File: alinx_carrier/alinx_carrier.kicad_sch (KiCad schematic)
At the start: 4 parts, among them J1 AXK6A2337YG, J2 AXK6A2337YG, J3 AXK6A2337YG, J4 AXK6A2337YG

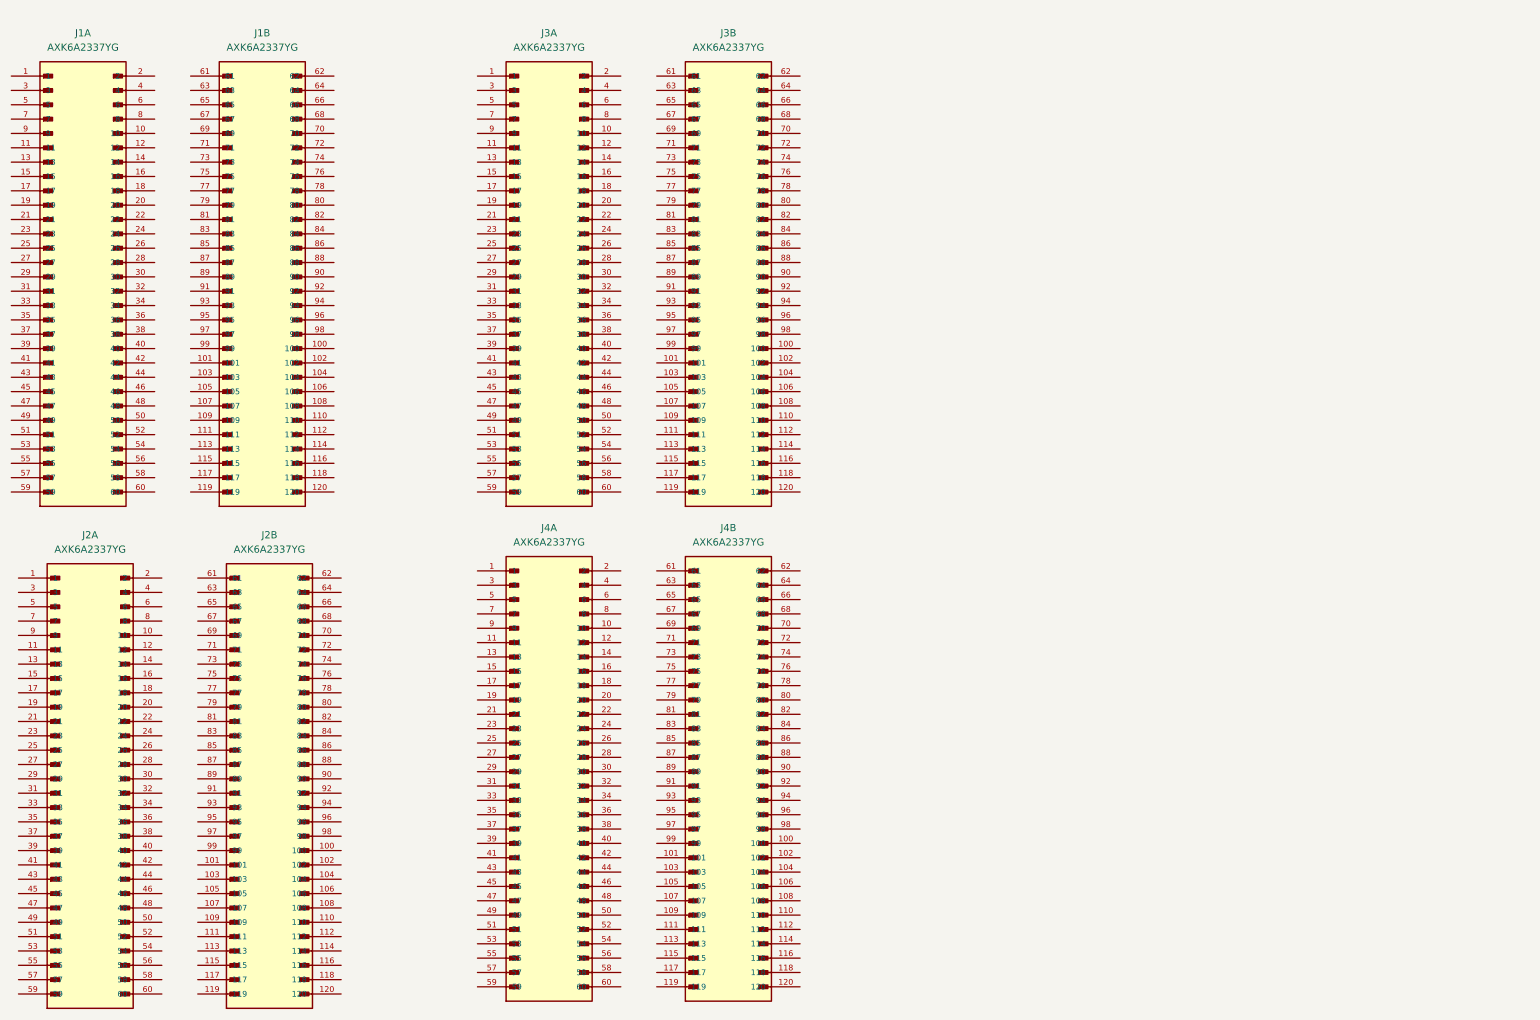
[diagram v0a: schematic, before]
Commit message: pulled in latest files froms snapeda for AXK6A2337YG
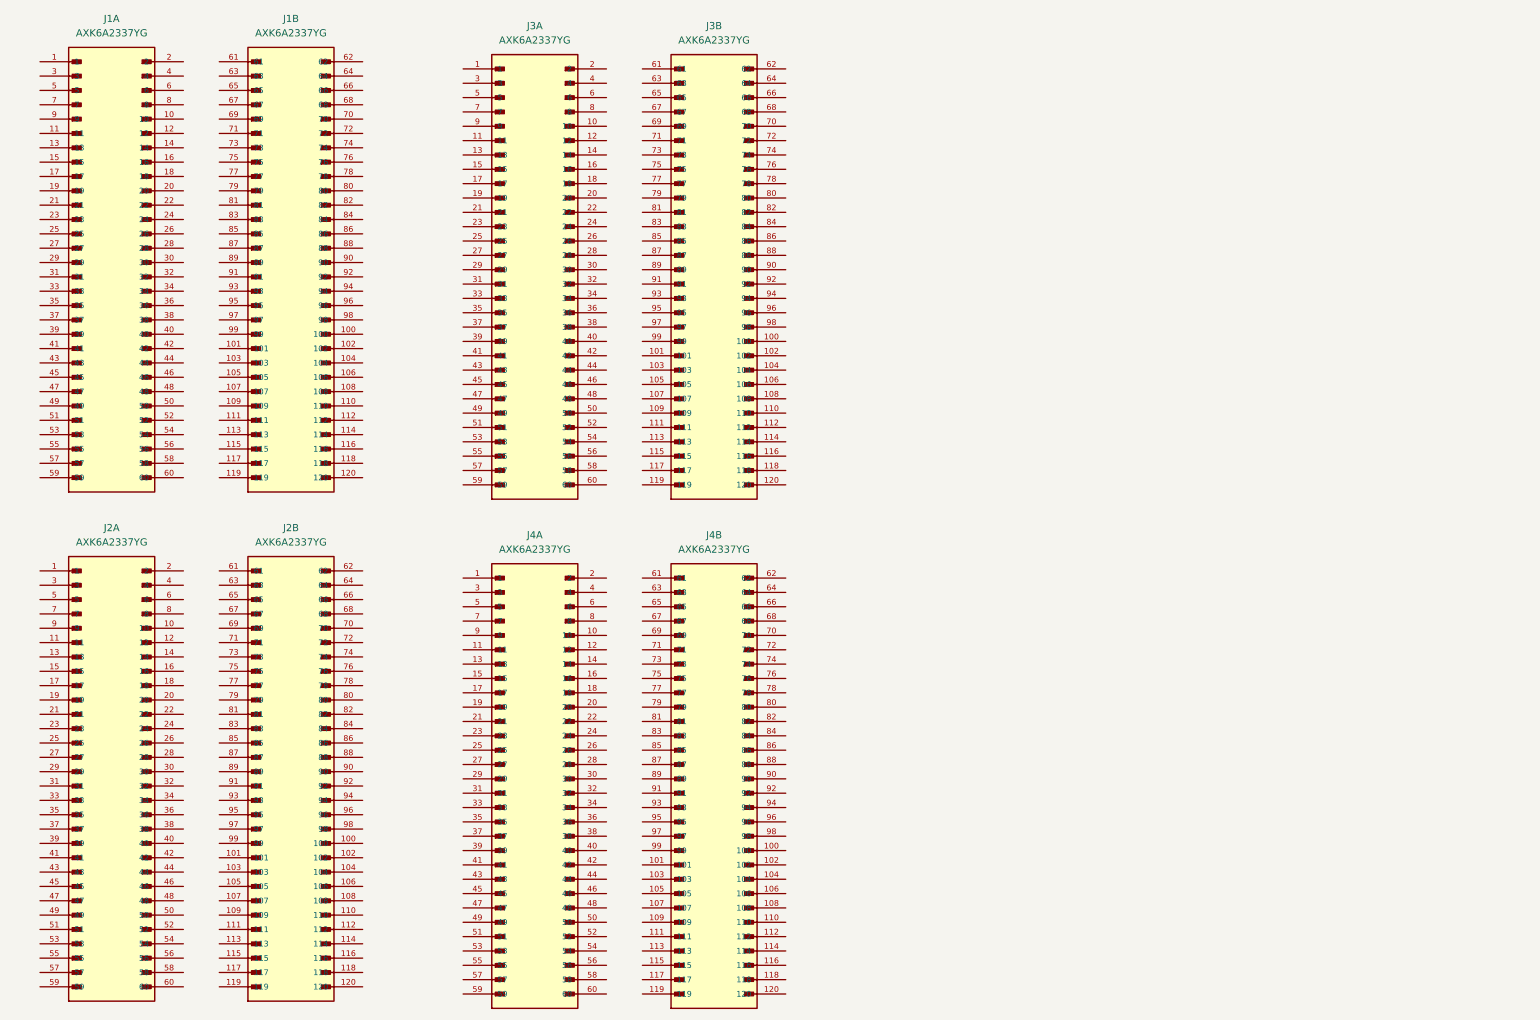
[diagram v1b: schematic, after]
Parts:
- J1, J2, J3, J4: footprint pedrolib:PANASONIC_AXK6A2337YG -> PANASONIC_AXK6A2337YG; AVAILABILITY (none) -> In Stock; DESCRIPTION (none) -> 120 Position Connector Header, Outer Shroud Contacts Surfac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; MANUFACTURER Panasonic -> (none); MAXIMUM_PACKAGE_HEIGHT 2.6mm -> (none); MF (none) -> Panasonic; MP (none) -> AXK6A2337YG; PACKAGE (none) -> None; PARTREV 2022.4 -> (none); PRICE (none) -> None; PURCHASE-URL (none) -> https://pricing.snapeda.com/search/part/AXK6A2337YG/?ref=eda; SNAPEDA_PN AXK6A2337YG -> (none); STANDARD Manufacturer Recommendations -> (none)

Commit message: added mounting holes to alinx carrier
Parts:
- added H1, H2, H3, H4: MountingHole_Pad, MountingHole:MountingHole_3mm_Pad_TopBottom, symbol Mechanical:MountingHole_Pad
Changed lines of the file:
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@@
     (pin "99")
+  )
+  (symbol (lib_id "Mechanical:MountingHole_Pad") (at 198.12 58.42 0) (unit 1)
+    (in_bom yes) (on_board yes) (fields_autoplaced)
+    (property "Reference" "H2" (id 0) (at 200.66 55.8799 0)
+      (effects (font (size 1.27 1.27)) (justify left))
+    )
+    (property "Value" "MountingHole_Pad" (id 1) (at 200.66 58.4199 0)
+      (effects (font (size 1.27 1.27)) (justify left))
+    )
+    (property "Footprint" "MountingHole:MountingHole_3mm_Pad_TopBottom" (id 2) (at 198.12 58.42 0)
+      (effects (font (size 1.27 1.27)) hide)
+    )
+    (property "Datasheet" "~" (id 3) (at 198.12 58.42 0)
+      (effects (font (size 1.27 1.27)) hide)
+    )
+    (pin "1")
   )
   (symbol (lib_id "pedrolib:AXK6A2337YG") (at 144.78 148.59 0) (unit 2)
@@
     (pin "99")
   )
+  (symbol (lib_id "Mechanical:MountingHole_Pad") (at 198.4161 40.9393 0) (unit 1)
+    (in_bom yes) (on_board yes) (fields_autoplaced)
+    (property "Reference" "H3" (id 0) (at 200.9561 38.3992 0)
+      (effects (font (size 1.27 1.27)) (justify left))
+    )
+    (property "Value" "MountingHole_Pad" (id 1) (at 200.9561 40.9392 0)
+      (effects (font (size 1.27 1.27)) (justify left))
+    )
+    (property "Footprint" "MountingHole:MountingHole_3mm_Pad_TopBottom" (id 2) (at 198.4161 40.9393 0)
+      (effects (font (size 1.27 1.27)) hide)
+    )
+    (property "Datasheet" "~" (id 3) (at 198.4161 40.9393 0)
+      (effects (font (size 1.27 1.27)) hide)
+    )
+    (pin "1")
+  )
+  (symbol (lib_id "Mechanical:MountingHole_Pad") (at 198.12 31.75 0) (unit 1)
+    (in_bom yes) (on_board yes) (fields_autoplaced)
+    (property "Reference" "H1" (id 0) (at 200.66 29.2099 0)
+      (effects (font (size 1.27 1.27)) (justify left))
+    )
+    (property "Value" "MountingHole_Pad" (id 1) (at 200.66 31.7499 0)
+      (effects (font (size 1.27 1.27)) (justify left))
+    )
+    (property "Footprint" "MountingHole:MountingHole_3mm_Pad_TopBottom" (id 2) (at 198.12 31.75 0)
+      (effects (font (size 1.27 1.27)) hide)
+    )
+    (property "Datasheet" "~" (id 3) (at 198.12 31.75 0)
+      (effects (font (size 1.27 1.27)) hide)
+    )
+    (pin "1")
+  )
+  (symbol (lib_id "Mechanical:MountingHole_Pad") (at 198.4161 49.53 0) (unit 1)
+    (in_bom yes) (on_board yes) (fields_autoplaced)
+    (property "Reference" "H4" (id 0) (at 200.9561 46.9899 0)
+      (effects (font (size 1.27 1.27)) (justify left))
+    )
+    (property "Value" "MountingHole_Pad" (id 1) (at 200.9561 49.5299 0)
+      (effects (font (size 1.27 1.27)) (justify left))
+    )
+    (property "Footprint" "MountingHole:MountingHole_3mm_Pad_TopBottom" (id 2) (at 198.4161 49.53 0)
+      (effects (font (size 1.27 1.27)) hide)
+    )
+    (property "Datasheet" "~" (id 3) (at 198.4161 49.53 0)
+      (effects (font (size 1.27 1.27)) hide)
+    )
+    (pin "1")
+  )
   (symbol (lib_id "pedrolib:AXK6A2337YG") (at 113.03 148.59 0) (unit 1)
     (in_bom yes) (on_board yes) (fields_autoplaced)
@@
   )
   (symbol_instances
+    (path "/bb425d40-cc47-4b23-914f-58366e05c30a"
+      (reference "H1") (unit 1) (value "MountingHole_Pad") (footprint "MountingHole:MountingHole_3mm_Pad_TopBottom")
+    )
+    (path "/914e5e89-7eaa-4d4c-8562-e97db0d3bcf8"
+      (reference "H2") (unit 1) (value "MountingHole_Pad") (footprint "MountingHole:MountingHole_3mm_Pad_TopBottom")
+    )
+    (path "/ae19385d-d6e1-4041-bce6-063446754b2d"
+      (reference "H3") (unit 1) (value "MountingHole_Pad") (footprint "MountingHole:MountingHole_3mm_Pad_TopBottom")
+    )
+    (path "/c422eb9d-35a6-4fd3-b837-58edeba25b00"
+      (reference "H4") (unit 1) (value "MountingHole_Pad") (footprint "MountingHole:MountingHole_3mm_Pad_TopBottom")
+    )
     (path "/3534d60f-9138-4da8-997e-7323e873752b"
       (reference "J1") (unit 1) (value "AXK6A2337YG") (footprint "PANASONIC_AXK6A2337YG")

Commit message: alinx carrier dimensions work
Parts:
- added J5: HR911130A, pedrolib:HANRUN_HR911130A, symbol pedrolib:HR911130A
- added U1: KSZ9031RNXCA, Package_DFN_QFN:QFN-48-1EP_7x7mm_P0.5mm_EP5.15x5.15mm, symbol Interface_Ethernet:KSZ9031RNXCA
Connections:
- new net: J5.S1 (SHIELD), J5.S2 (SHIELD)
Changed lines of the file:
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@@
     (pin "99")
+  )
+  (symbol (lib_id "Interface_Ethernet:KSZ9031RNXCA") (at 223.52 118.11 0) (unit 1)
+    (in_bom yes) (on_board yes) (fields_autoplaced)
+    (property "Reference" "U1" (id 0) (at 235.6994 158.75 0)
+      (effects (font (size 1.27 1.27)) (justify left))
+    )
+    (property "Value" "KSZ9031RNXCA" (id 1) (at 235.6994 161.29 0)
+      (effects (font (size 1.27 1.27)) (justify left))
+    )
+    (property "Footprint" "Package_DFN_QFN:QFN-48-1EP_7x7mm_P0.5mm_EP5.15x5.15mm" (id 2) (at 234.95 157.48 0)
+      (effects (font (size 1.27 1.27)) (justify left) hide)
+    )
+    (property "Datasheet" "http://ww1.microchip.com/downloads/en/DeviceDoc/00002117C.pdf" (id 3) (at 223.52 160.02 0)
+      (effects (font (size 1.27 1.27)) hide)
+    )
+    (pin "1")
+    (pin "10")
+    (pin "11")
+    (pin "12")
+    (pin "13")
+    (pin "14")
+    (pin "15")
+    (pin "16")
+    (pin "17")
+    (pin "18")
+    (pin "19")
+    (pin "2")
+    (pin "20")
+    (pin "21")
+    (pin "22")
+    (pin "23")
+    (pin "24")
+    (pin "25")
+    (pin "26")
+    (pin "27")
+    (pin "28")
+    (pin "29")
+    (pin "3")
+    (pin "30")
+    (pin "31")
+    (pin "32")
+    (pin "33")
+    (pin "34")
+    (pin "35")
+    (pin "36")
+    (pin "37")
+    (pin "38")
+    (pin "39")
+    (pin "4")
+    (pin "40")
+    (pin "41")
+    (pin "42")
+    (pin "43")
+    (pin "44")
+    (pin "45")
+    (pin "46")
+    (pin "47")
+    (pin "48")
+    (pin "49")
+    (pin "5")
+    (pin "6")
+    (pin "7")
+    (pin "8")
+    (pin "9")
   )
   (symbol (lib_id "Mechanical:MountingHole_Pad") (at 198.12 58.42 0) (unit 1)
@@
     (pin "1")
   )
+  (symbol (lib_id "pedrolib:HR911130A") (at 267.97 46.99 0) (unit 1)
+    (in_bom yes) (on_board yes) (fields_autoplaced)
+    (property "Reference" "J5" (id 0) (at 276.86 46.9899 0)
+      (effects (font (size 1.27 1.27)) (justify left))
+    )
+    (property "Value" "HR911130A" (id 1) (at 276.86 49.5299 0)
+      (effects (font (size 1.27 1.27)) (justify left))
+    )
+    (property "Footprint" "pedrolib:HANRUN_HR911130A" (id 2) (at 267.97 46.99 0)
+      (effects (font (size 1.27 1.27)) (justify bottom) hide)
+    )
+    (property "Datasheet" "" (id 3) (at 267.97 46.99 0)
+      (effects (font (size 1.27 1.27)) hide)
+    )
+    (property "MANUFACTURER" "HanRun" (id 4) (at 267.97 46.99 0)
+      (effects (font (size 1.27 1.27)) (justify bottom) hide)
+    )
+    (property "MAXIMUM_PACKAGE_HEIGHT" "13.75 mm" (id 5) (at 267.97 46.99 0)
+      (effects (font (size 1.27 1.27)) (justify bottom) hide)
+    )
+    (property "PARTREV" "A" (id 6) (at 267.97 46.99 0)
+      (effects (font (size 1.27 1.27)) (justify bottom) hide)
+    )
+    (property "STANDARD" "Manufacturer Recommendations" (id 7) (at 267.97 46.99 0)
+      (effects (font (size 1.27 1.27)) (justify bottom) hide)
+    )
+    (pin "1")
+    (pin "10")
+    (pin "11")
+    (pin "12")
+    (pin "13")
+    (pin "14")
+    (pin "2")
+    (pin "3")
+    (pin "4")
+    (pin "5")
+    (pin "6")
+    (pin "7")
+    (pin "8")
+    (pin "9")
+    (pin "S1")
+    (pin "S2")
+  )
   (symbol (lib_id "Mechanical:MountingHole_Pad") (at 198.12 31.75 0) (unit 1)
     (in_bom yes) (on_board yes) (fields_autoplaced)
@@
       (reference "J4") (unit 2) (value "AXK6A2337YG") (footprint "PANASONIC_AXK6A2337YG")
     )
-  )
+    (path "/b90ef20e-83a4-4cdc-92a2-863169f9de24"
+      (reference "J5") (unit 1) (value "HR911130A") (footprint "pedrolib:HANRUN_HR911130A")
+    )
+    (path "/9065dace-acc0-4d8a-aee4-0c5661dd9b8d"
+      (reference "U1") (unit 1) (value "KSZ9031RNXCA") (footprint "Package_DFN_QFN:QFN-48-1EP_7x7mm_P0.5mm_EP5.15x5.15mm")
+    )
+  )

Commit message: put some usb-c stuff on the alinx carrier
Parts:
- added J6: USB4105-GF-A, pedrolib:GCT_USB4105-GF-A, symbol pedrolib:USB4105-GF-A
- added U2: STUSB4500QTR, Package_DFN_QFN:QFN-24-1EP_4x4mm_P0.5mm_EP2.7x2.7mm, symbol Interface_USB:STUSB4500QTR
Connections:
- new net: U2.10 (GND), U2.25 (GND)
- new net: J6.A1_B12 (GND), J6.B1_A12 (GND)
- new net: J6.A4_B9 (VBUS), J6.B4_A9 (VBUS)
- new net: J6.S1 (SHELL_GND), J6.S2 (SHELL_GND), J6.S3 (SHELL_GND), J6.S4 (SHELL_GND)
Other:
- moved on the sheet: H1, H2, H3, H4, J5, U1

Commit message: added jtag connector
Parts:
- added J7: 87832-1420, pedrolib:MOLEX_87832-1420, symbol pedrolib:87832-1420
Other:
- moved on the sheet: J6, U2
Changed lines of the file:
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@@
     (pin "99")
+  )
+  (symbol (lib_id "pedrolib:87832-1420") (at 257.81 104.14 0) (unit 1)
+    (in_bom yes) (on_board yes) (fields_autoplaced)
+    (property "Reference" "J7" (id 0) (at 256.54 88.9 0))
+    (property "Value" "87832-1420" (id 1) (at 256.54 91.44 0))
+    (property "Footprint" "pedrolib:MOLEX_87832-1420" (id 2) (at 256.54 118.11 0)
+      (effects (font (size 1.27 1.27)) (justify bottom) hide)
+    )
+    (property "Datasheet" "" (id 3) (at 257.81 104.14 0)
+      (effects (font (size 1.27 1.27)) hide)
+    )
+    (property "MANUFACTURER" "MOLEX" (id 4) (at 257.81 104.14 0)
+      (effects (font (size 1.27 1.27)) (justify bottom) hide)
+    )
+    (pin "1")
+    (pin "10")
+    (pin "11")
+    (pin "12")
+    (pin "13")
+    (pin "14")
+    (pin "2")
+    (pin "3")
+    (pin "4")
+    (pin "5")
+    (pin "6")
+    (pin "7")
+    (pin "8")
+    (pin "9")
   )
   (symbol (lib_id "pedrolib:AXK6A2337YG") (at 113.03 58.42 0) (unit 1)
@@
     (pin "99")
   )
-  (symbol (lib_id "Interface_USB:STUSB4500QTR") (at 209.55 134.62 0) (unit 1)
-    (in_bom yes) (on_board yes) (fields_autoplaced)
-    (property "Reference" "U2" (id 0) (at 211.5694 157.48 0)
-      (effects (font (size 1.27 1.27)) (justify left))
-    )
-    (property "Value" "STUSB4500QTR" (id 1) (at 211.5694 160.02 0)
-      (effects (font (size 1.27 1.27)) (justify left))
-    )
-    (property "Footprint" "Package_DFN_QFN:QFN-24-1EP_4x4mm_P0.5mm_EP2.7x2.7mm" (id 2) (at 209.55 134.62 0)
-      (effects (font (size 1.27 1.27)) hide)
-    )
-    (property "Datasheet" "https://www.st.com/resource/en/datasheet/stusb4500.pdf" (id 3) (at 209.55 134.62 0)
+  (symbol (lib_id "Interface_USB:STUSB4500QTR") (at 208.28 138.43 0) (unit 1)
+    (in_bom yes) (on_board yes) (fields_autoplaced)
+    (property "Reference" "U2" (id 0) (at 210.2994 161.29 0)
+      (effects (font (size 1.27 1.27)) (justify left))
+    )
+    (property "Value" "STUSB4500QTR" (id 1) (at 210.2994 163.83 0)
+      (effects (font (size 1.27 1.27)) (justify left))
+    )
+    (property "Footprint" "Package_DFN_QFN:QFN-24-1EP_4x4mm_P0.5mm_EP2.7x2.7mm" (id 2) (at 208.28 138.43 0)
+      (effects (font (size 1.27 1.27)) hide)
+    )
+    (property "Datasheet" "https://www.st.com/resource/en/datasheet/stusb4500.pdf" (id 3) (at 208.28 138.43 0)
       (effects (font (size 1.27 1.27)) hide)
     )
@@
     (pin "1")
   )
-  (symbol (lib_id "pedrolib:USB4105-GF-A") (at 248.92 133.35 0) (unit 1)
-    (in_bom yes) (on_board yes) (fields_autoplaced)
-    (property "Reference" "J6" (id 0) (at 248.92 115.57 0))
-    (property "Value" "USB4105-GF-A" (id 1) (at 248.92 118.11 0))
-    (property "Footprint" "pedrolib:GCT_USB4105-GF-A" (id 2) (at 248.92 133.35 0)
-      (effects (font (size 1.27 1.27)) (justify bottom) hide)
-    )
-    (property "Datasheet" "" (id 3) (at 248.92 133.35 0)
-      (effects (font (size 1.27 1.27)) hide)
-    )
-    (property "PARTREV" "A3" (id 4) (at 248.92 133.35 0)
-      (effects (font (size 1.27 1.27)) (justify bottom) hide)
-    )
-    (property "MANUFACTURER" "GCT" (id 5) (at 248.92 133.35 0)
-      (effects (font (size 1.27 1.27)) (justify bottom) hide)
-    )
-    (property "MAXIMUM_PACKAGE_HEIGHT" "3.31 mm" (id 6) (at 248.92 133.35 0)
-      (effects (font (size 1.27 1.27)) (justify bottom) hide)
-    )
-    (property "STANDARD" "Manufacturer Recommendations" (id 7) (at 248.92 133.35 0)
+  (symbol (lib_id "pedrolib:USB4105-GF-A") (at 252.73 146.05 0) (unit 1)
+    (in_bom yes) (on_board yes) (fields_autoplaced)
+    (property "Reference" "J6" (id 0) (at 252.73 128.27 0))
+    (property "Value" "USB4105-GF-A" (id 1) (at 252.73 130.81 0))
+    (property "Footprint" "pedrolib:GCT_USB4105-GF-A" (id 2) (at 252.73 146.05 0)
+      (effects (font (size 1.27 1.27)) (justify bottom) hide)
+    )
+    (property "Datasheet" "" (id 3) (at 252.73 146.05 0)
+      (effects (font (size 1.27 1.27)) hide)
+    )
+    (property "PARTREV" "A3" (id 4) (at 252.73 146.05 0)
+      (effects (font (size 1.27 1.27)) (justify bottom) hide)
+    )
+    (property "MANUFACTURER" "GCT" (id 5) (at 252.73 146.05 0)
+      (effects (font (size 1.27 1.27)) (justify bottom) hide)
+    )
+    (property "MAXIMUM_PACKAGE_HEIGHT" "3.31 mm" (id 6) (at 252.73 146.05 0)
+      (effects (font (size 1.27 1.27)) (justify bottom) hide)
+    )
+    (property "STANDARD" "Manufacturer Recommendations" (id 7) (at 252.73 146.05 0)
       (effects (font (size 1.27 1.27)) (justify bottom) hide)
     )
@@
       (reference "J6") (unit 1) (value "USB4105-GF-A") (footprint "pedrolib:GCT_USB4105-GF-A")
     )
+    (path "/3e13a8fb-636d-48cc-8f01-28ee96a345dc"
+      (reference "J7") (unit 1) (value "87832-1420") (footprint "pedrolib:MOLEX_87832-1420")
+    )
     (path "/9065dace-acc0-4d8a-aee4-0c5661dd9b8d"
